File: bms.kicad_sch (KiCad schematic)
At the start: 62 parts, among them J10 SOLAR, Q10 SI2308, Q11 CSD17577Q3A, Q7 CSD18512Q5B, Q8 CSD18512Q5B, Q9 SI2308, SW3 POWER/RESET, U8 BQ25798

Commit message: lots of fixes!
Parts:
- removed C134: 10nF, Capacitor_SMD:C_0402_1005Metric, symbol Device:C_Small
- removed C35, C57, C59, C60, C63, C65, C71, C73, C74, C82, C84, C85, C86, C87, C88, C90, C92: 10uF, Capacitor_SMD:C_1206_3216Metric, symbol Device:C_Small
- removed C62, C79: 2.2uF, Capacitor_SMD:C_0805_2012Metric, symbol Device:C_Small
- removed C64, C72, C80, C89, C91: 100nF, Capacitor_SMD:C_0402_1005Metric, symbol Device:C_Small
- removed C75, C76, C77: 47nF, Capacitor_SMD:C_0402_1005Metric, symbol Device:C_Small
- removed C78: 4.7uF, Capacitor_SMD:C_0603_1608Metric, symbol Device:C_Small
- removed C81, C83: 1nF, Capacitor_SMD:C_0402_1005Metric_Pad0.74x0.62mm_HandSolder, symbol Device:C_Small
- removed D7: SMF24A, Diode_SMD:D_SOD-123F, symbol Diode:SMF24A
- removed D8: CHARGING, LED_SMD:LED_0805_2012Metric, symbol Device:LED
- removed D9: SS36B, Diode_SMD:D_SMB, symbol Device:D_Schottky
- removed J10: SOLAR, Connector_JST:JST_PH_S2B-PH-SM4-TB_1x02-1MP_P2.00mm_Horizontal, symbol Connector:Conn_01x02_Socket
- removed L1: 2.2uH, Inductor_SMD:L_Vishay_IFSC-1515AH_4x4x1.8mm, symbol Device:L
- removed Q10, Q9: SI2308, Package_TO_SOT_SMD:SOT-23, symbol Transistor_FET:Q_NMOS_GSD
- removed Q11: CSD17577Q3A, Package_SON:VSON-8_3.3x3.3mm_P0.65mm_NexFET, symbol Transistor_FET:CSD17581Q3A
- removed Q7, Q8: CSD18512Q5B, Package_SON:VSONP-8-1EP_5x6_P1.27mm, symbol Transistor_FET:Q_NMOS_DGS
- removed R49, R62: 2, Resistor_SMD:R_0402_1005Metric, symbol Device:R_Small
- removed R51: 5.23k, Resistor_SMD:R_0603_1608Metric_Pad0.98x0.95mm_HandSolder, symbol Device:R_Small
- removed R52: 30.1k, Resistor_SMD:R_0603_1608Metric_Pad0.98x0.95mm_HandSolder, symbol Device:R_Small
- removed R53, R57, R60, R61: 294, Resistor_SMD:R_0402_1005Metric, symbol Device:R_Small
- removed R54: 24.3k, Resistor_SMD:R_0603_1608Metric_Pad0.98x0.95mm_HandSolder, symbol Device:R_Small
- removed R55: 68.1k, Resistor_SMD:R_0603_1608Metric_Pad0.98x0.95mm_HandSolder, symbol Device:R_Small
- removed R56: 100k, Resistor_SMD:R_0402_1005Metric, symbol Device:R_Small
- removed R58: 8.2k, Resistor_SMD:R_0402_1005Metric_Pad0.72x0.64mm_HandSolder, symbol Device:R_Small
- removed R59, R63: 100, Resistor_SMD:R_0402_1005Metric, symbol Device:R_Small
- removed R64, R65: 2.2, Resistor_SMD:R_0402_1005Metric_Pad0.72x0.64mm_HandSolder, symbol Device:R_Small
- removed R66: 3k, Resistor_SMD:R_0402_1005Metric_Pad0.72x0.64mm_HandSolder, symbol Device:R_Small
- removed SW3: POWER/RESET, Button_Switch_SMD:SW_Push_SPST_NO_Alps_SKRK, symbol Switch:SW_Push
- removed TH5: 103AT 10k, Resistor_SMD:R_0603_1608Metric, symbol Device:Thermistor_NTC
- removed TP4: PPHV, TestPoint:TestPoint_2Pads_Pitch2.54mm_Drill0.8mm, symbol Connector:TestPoint_2Pole
- removed U8: BQ25798, Package_DFN_QFN:Texas_RQM0029A_VQFN-29_4x4mm_P0.4mm, symbol Battery_Management:BQ25798
- added BT1, BT2: 21700 Li-ion, easyeda2kicad:BAT-SMD_L82.5.5-W25-BH-21700-B1BJ001, symbol Device:Battery_Cell
- added C105, C132, C47, C98: 10nF, Capacitor_SMD:C_0402_1005Metric, symbol Device:C_Small
- added C48, C67, C68, C69, C70: 10uF, Capacitor_SMD:C_0805_2012Metric, symbol Device:C_Small
- added C49, C50, C51, C54, C61, C66: 100nF, Capacitor_SMD:C_0402_1005Metric, symbol Device:C_Small
- added C52: 1uF, Capacitor_SMD:C_0402_1005Metric, symbol Device:C_Small
- added C53, C55, C56, C58: 0.47uF, Capacitor_SMD:C_0402_1005Metric, symbol Device:C_Small
- added D23: BAT54S, Package_TO_SOT_SMD:SOT-23, symbol Diode:BAT54S
- added D5: SMF10A, Diode_SMD:D_SOD-123, symbol Diode:SMF10A
- added D6: BZX585-C15,135, Diode_SMD:D_SOD-523, symbol Device:D_Zener
- added F5: 10A hold, Fuse:Fuse_2920_7451Metric, symbol Device:Polyfuse
- added J9: BAT_PORT, Connector_Molex:Molex_PicoBlade_53261-0271_1x02-1MP_P1.25mm_Horizontal, symbol Connector_Generic_MountingPin:Conn_01x02_MountingPin
- added JP7: ZVC, Jumper:SolderJumper-2_P1.3mm_Open_RoundedPad1.0x1.5mm, symbol Jumper:SolderJumper_2_Open
- added Q16: TPN2R203NC, easyeda2kicad:TSON-8_L3.1-W3.1-P0.65-LS3.3-BL-EP, symbol Transistor_FET:CSD17581Q3A
- added Q5, Q6: AON7544, easyeda2kicad:PQFN-8_L3.1-W3.1-P0.65-LS3.3-BL, symbol easyeda2kicad:AON7534-ES
- added R135, R46, R50: 10k, Resistor_SMD:R_0402_1005Metric, symbol Device:R_Small
- added R39, R40: 150, Resistor_SMD:R_1206_3216Metric, symbol Device:R_Small
- added R41: 5m, footprints:R_Shunt_0805_2012Metric_Kelvin, symbol Device:R_Shunt
- added R42: 10, Resistor_SMD:R_0402_1005Metric, symbol Device:R_Small
- added R43, R45: 1k, Resistor_SMD:R_0402_1005Metric, symbol Device:R_Small
- added R44, R48: 100, Resistor_SMD:R_0402_1005Metric, symbol Device:R_Small
- added R47: 330, Resistor_SMD:R_1210_3225Metric, symbol Device:R_Small
- added TH1, TH2, TH3, TH4: 103AT 10k, Resistor_SMD:R_0603_1608Metric, symbol Device:Thermistor_NTC
- added TP1: R_SENSE_SHUNT, TestPoint:TestPoint_2Pads_Pitch2.54mm_Drill0.8mm, symbol Connector:TestPoint_2Pole
- added TP2: IN_CP, TestPoint:TestPoint_2Pads_Pitch2.54mm_Drill0.8mm, symbol Connector:TestPoint_2Pole
- added TP3: REG3, TestPoint:TestPoint_Pad_D1.0mm, symbol Connector:TestPoint_Probe
- added U7: MAX17320G22+, easyeda2kicad:QFN-24_L4.0-W4.0-P0.50-BL-EP2.6, symbol easyeda2kicad:MAX17320G22+
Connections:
- net +PACK: now also C61.2, C66.1, C67.1, C68.1, C69.1, C70.1, Q6.1 (S), Q6.2 (S), Q6.3 (S), R45.2, R47.2
- net GND: now also C67.2, C68.2, C69.2, C70.2, R41.4, TP1.2
- new net: C98.1, TH1.1, U7.16 (TH2)
- new net: BT2.2 (-), J9.1 (Pin_1), Q16.5 (D), Q16.6 (D), Q16.7 (D), Q16.8 (D), Q16.9 (D)
- new net: BT1.1 (+), F5.1, J9.2 (Pin_2), R135.1, R40.1, R42.1
- new net: JP7.1 (A), U7.5 (ZVC)
- new net: JP7.2 (B), R47.1
- new net: R48.1, U7.4 (DIS)
- new net: Q6.4 (G), R48.2
- new net: C56.2, TP3.1, U7.13 (REG3)
- new net: C47.1, TH4.1, U7.10 (TH1)
- new net: D6.1 (K), Q16.4 (G), R135.2
- new net: C105.1, TH3.1, U7.18 (TH3)
- new net: R50.1, U7.7 (ALRT)
- new net: C132.1, TH2.1, U7.19 (TH4)
- new net: BT1.2 (-), BT2.1 (+), R39.1
- new net: C49.2, C50.1, D23.3 (COM), R39.2, U7.21 (CELL1)
- new net: R45.1, U7.6 (PCKP)
- new net: R43.1, U7.11 (PFAIL)
- new net: C58.1, R46.1, U7.12 (AOLDO)
- new net: R41.3, U7.14 (CSN)
- new net: R41.2, U7.15 (CSP)
- new net: C55.2, U7.17 (REG2)
- new net: C53.2, TP2.2, U7.2 (CP)
- new net: C49.1, C51.1, R40.2, U7.22 (CELL2), U7.23 (CELL3), U7.24 (BATTS)
- new net: R44.1, U7.3 (CHG)
- new net: Q5.5 (D), Q5.6 (D), Q5.7 (D), Q5.8 (D), Q6.5 (D), Q6.6 (D), Q6.7 (D), Q6.8 (D)
- new net: C54.2, Q5.4 (G), R44.2
- new net +3V3: R50.2
- new net +BATT: C48.1, C54.1, C61.1, D5.1 (A1), F5.2, Q5.1 (S), Q5.2 (S), Q5.3 (S)
- new net -BATT: C105.2, C132.2, C47.2, C48.2, C50.2, C51.2, C52.2, C55.1, C56.1, C58.2, C66.2, C98.2, D23.1 (A), D5.2 (A2), D6.2 (A), Q16.1 (S), Q16.2 (S), Q16.3 (S), R41.1, R43.2, R46.2, TH1.2, TH2.2, TH3.2, TH4.2, TP1.1, U7.20 (GND), U7.25 (EP)
- new net BMS_IN: C52.1, C53.1, D23.2 (K), R42.2, TP2.1, U7.1 (IN)
- new net I2C_HOST_SCL: U7.8 (SCL/DOD)
- new net I2C_HOST_SDA: U7.9 (SDA/DQ)
- no-connect marks 2 -> 1
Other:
- note added: "10nF noise filtering capacitors"
- note added: "Battery Management System (BMS)"
- note removed: "4 x 10uF 1206"
- note removed: "5 x 10uF 1210"
- note removed: "Capacitors voltage ratings specified, generally >25V - use XR7/C0G"
- note removed: "Charge Controller"
- note removed: "VSYS from 7.1V - 8.8V for 2S, max ~6A"
- title: Battery Charge Controller -> Battery Managment System (BMS)

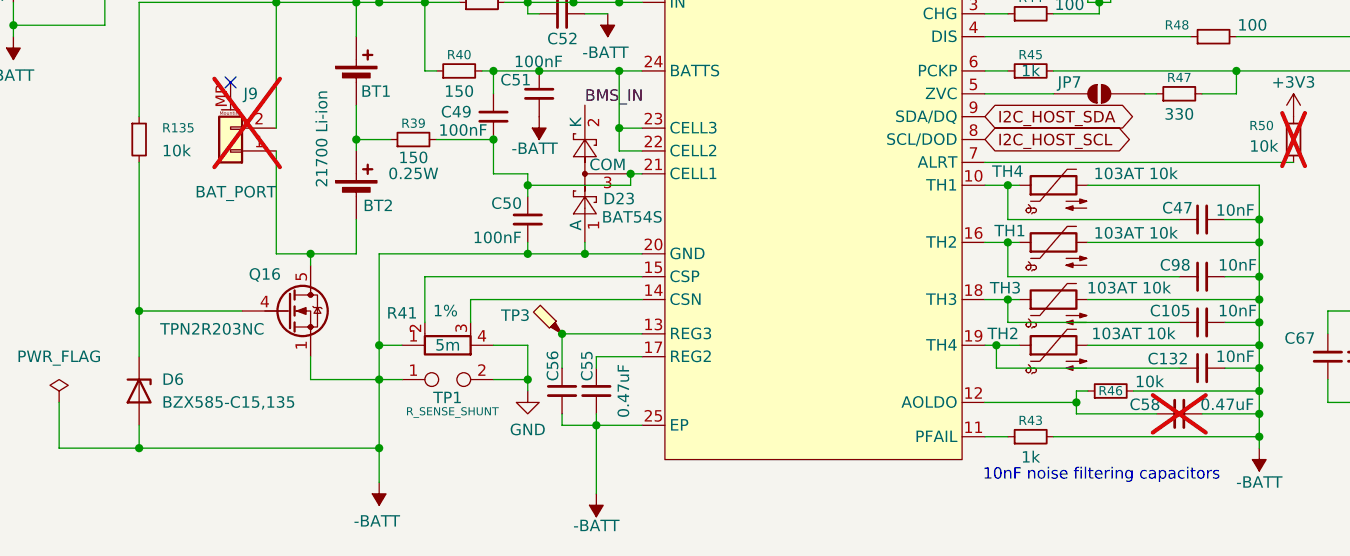
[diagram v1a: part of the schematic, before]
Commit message: organize part fields
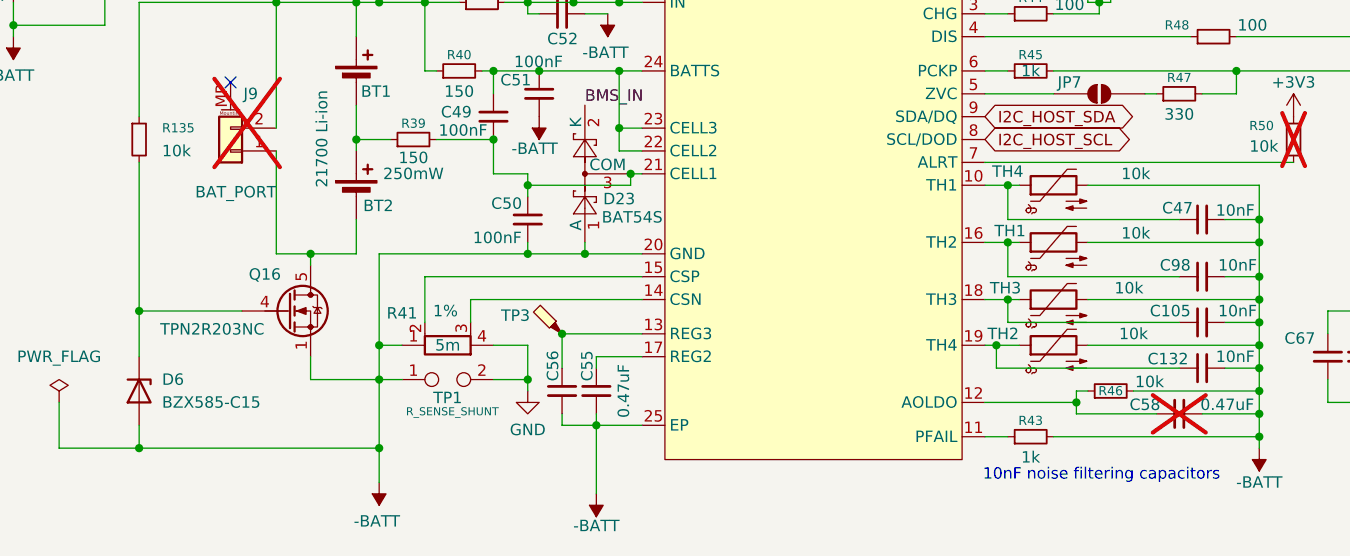
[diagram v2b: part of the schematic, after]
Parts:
- BT1, BT2: MPN (none) -> BH-21700-B1BJ001; Manufacturer (none) -> MYOUNG
- C105, C132, C47, C98: Dielectric (none) -> X7R; MPN (none) -> TCC0402X7R103M500AT; Manufacturer (none) -> CCTC; Tolerance (none) -> 20%
- C48: Dielectric (none) -> X5R; MPN (none) -> CGA0805X5R106M500MT; Manufacturer (none) -> HRE; Tolerance (none) -> 20%
- C49, C51, C61, C66: Capacitor Rating X7R -> (none); Dielectric (none) -> X7R; MPN (none) -> 0402B104J500NT; Manufacturer (none) -> FH (Fenghua); Tolerance (none) -> 5%
- C50, C54: Capacitor Rating X7R -> (none); Dielectric (none) -> X7R; MPN (none) -> 0402B104J500NT; Manufacturer (none) -> FH (Fenghua); Tolerance (none) -> 5%; Voltage Rating 25V -> 50V
- C52: Dielectric (none) -> X5R; MPN (none) -> HGC0402R5105K500NTEJ; Manufacturer (none) -> Chinocera; Tolerance (none) -> 10%
- C53, C55: Dielectric (none) -> X5R; MPN (none) -> HGC0402R5474K250NTEJ; Manufacturer (none) -> Chinocera; Tolerance (none) -> 10%
- C56, C58: Dielectric (none) -> X5R; MPN (none) -> HGC0402R5474K250NTEJ; Manufacturer (none) -> Chinocera; Tolerance (none) -> 10%; Voltage Rating 16V -> 25V
- C67, C68, C69, C70: Dielectric (none) -> X5R; MPN (none) -> CGA0805X5R106M500MT; Manufacturer (none) -> HRE; Tolerance (none) -> 20%; Voltage Rating 25V -> 50V
- D23: MPN (none) -> BAT54SLT1G; Manufacturer (none) -> onsemi
- D5: MPN (none) -> SMF10A; Manufacturer (none) -> AnBon
- D6: value BZX585-C15,135 -> BZX585-C15; MPN (none) -> BZX585-C15,135; Manufacturer (none) -> Nexperia
- F5: MPN (none) -> BSMD2920L-1000-21V; Manufacturer (none) -> BHFUSE
- J9: MPN (none) -> 1.25-2PWB; Manufacturer (none) -> DEALON
- Q16: MPN (none) -> TPN2R203NC,L1Q(M; Manufacturer (none) -> Toshiba
- Q5, Q6: Manufacturer (none) -> Alpha & Omega Semiconductor
- R135, R46, R50: MPN (none) -> FRH0402D1002TS; Manufacturer (none) -> FOJAN; Power Rating (none) -> 62.5mW; Tolerance (none) -> 0.5%
- R39: MPN (none) -> RT1206BRD07150RL; Manufacturer (none) -> YAGEO; Power Rating 0.25W -> 250mW; Tolerance (none) -> 0.1%
- R40: MPN (none) -> RT1206BRD07150RL; Manufacturer (none) -> YAGEO; Power Rating (none) -> 250mW; Tolerance (none) -> 0.1%
- R41: MPN (none) -> YHR0805SE1DR005F5; Manufacturer (none) -> Yohey; Power Rating (none) -> 500mW
- R42: MPN (none) -> 1RC0402F1009; Manufacturer (none) -> SAE; Power Rating (none) -> 62.5mW; Tolerance (none) -> 1%
- R43, R45: MPN (none) -> FRH0402B1001TS; Manufacturer (none) -> FOJAN; Power Rating (none) -> 62.5mW; Tolerance (none) -> 0.1%
- R44, R48: MPN (none) -> FRH0402D1000TS; Manufacturer (none) -> FOJAN; Power Rating (none) -> 62.5mW; Tolerance (none) -> 0.5%
- R47: MPN (none) -> FRP1210F3300TS; Manufacturer (none) -> FOJAN; Tolerance (none) -> 1%
- TH1, TH2, TH3, TH4: value 103AT 10k -> 10k; MPN (none) -> NCU18XH103D60RB; Manufacturer (none) -> Murata; Tolerance (none) -> 0.5%
- U7: Manufacturer ADI(亚德诺)/MAXIM(美信) -> Analog Devices (Maxim)

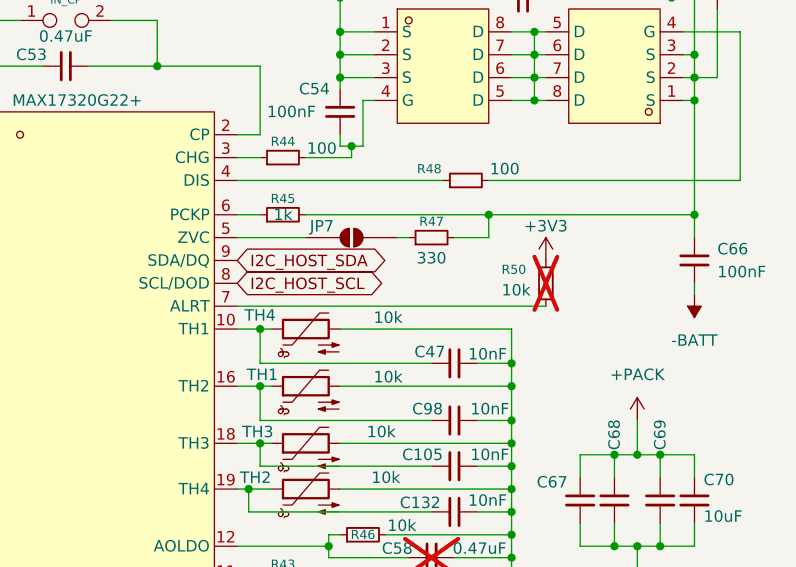
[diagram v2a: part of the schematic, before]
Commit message: add extra PWR_FLAGs
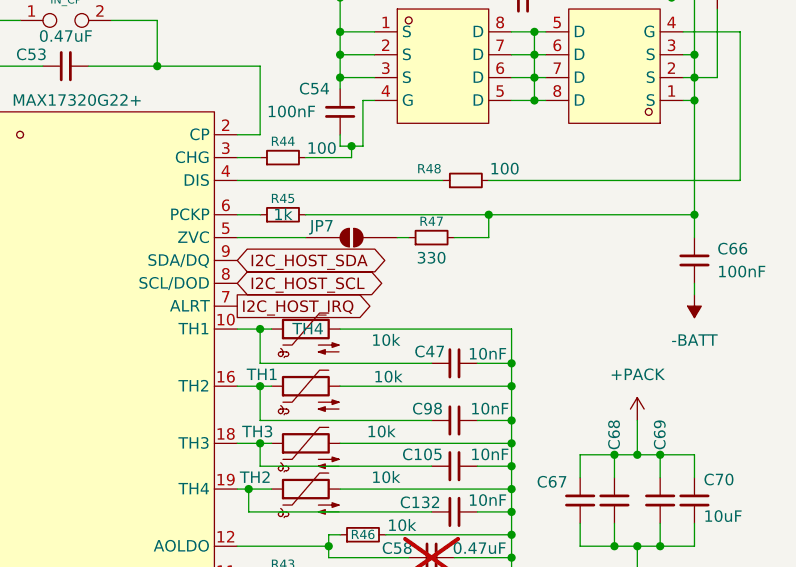
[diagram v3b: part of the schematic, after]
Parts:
- removed R50: 10k, Resistor_SMD:R_0402_1005Metric, symbol Device:R_Small
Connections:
- net I2C_HOST_IRQ: now reaches U7.7 (ALRT)
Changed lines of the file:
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@@
 	(wire
 		(pts
-			(xy 205.74 104.14) (xy 171.45 104.14)
-		)
-		(stroke
-			(width 0)
-			(type default)
-		)
-	)
-	(wire
-		(pts
 			(xy 116.84 93.98) (xy 116.84 96.52)
 		)
@@
 		)
 	)
+	(global_label "I2C_HOST_IRQ"
+		(shape output)
+		(at 171.45 104.14 0)
+		(fields_autoplaced yes)
+		(effects
+			(font
+				(size 1.27 1.27)
+			)
+			(justify left)
+		)
+		(property "Intersheetrefs" "${INTERSHEET_REFS}"
+			(at 187.4981 104.14 0)
+			(hide yes)
+			(show_name no)
+			(do_not_autoplace no)
+			(effects
+				(font
+					(size 1.27 1.27)
+				)
+				(justify left)
+			)
+		)
+	)
 	(global_label "I2C_HOST_SDA"
 		(shape bidirectional)
@@
 	)
 	(symbol
-		(lib_id "Device:R_Small")
-		(at 205.74 101.6 180)
-		(unit 1)
-		(body_style 1)
-		(exclude_from_sim no)
-		(in_bom yes)
-		(on_board yes)
-		(in_pos_files yes)
-		(dnp yes)
-		(property "Reference" "R50"
-			(at 202.184 100.076 0)
-			(show_name no)
-			(do_not_autoplace no)
-			(effects
-				(font
-					(size 1.016 1.016)
-				)
-			)
-		)
-		(property "Value" "10k"
-			(at 202.438 102.362 0)
-			(show_name no)
-			(do_not_autoplace no)
-			(effects
-				(font
-					(size 1.27 1.27)
-				)
-			)
-		)
-		(property "Footprint" "Resistor_SMD:R_0402_1005Metric"
-			(at 205.74 101.6 0)
-			(hide yes)
-			(show_name no)
-			(do_not_autoplace no)
-			(effects
-				(font
-					(size 1.27 1.27)
-				)
-			)
-		)
-		(property "Datasheet" "https://datasheet.lcsc.com/datasheet/pdf/68379ec060dbf46ca58f0ea52f41dfcd.pdf?productCode=C54951138"
-			(at 205.74 101.6 0)
-			(hide yes)
-			(show_name no)
-			(do_not_autoplace no)
-			(effects
-				(font
-					(size 1.27 1.27)
-				)
-			)
-		)
-		(property "Description" "RES 10kΩ ±0.5% 62.5mW 0402 thick film"
-			(at 205.74 101.6 0)
-			(hide yes)
-			(show_name no)
-			(do_not_autoplace no)
-			(effects
-				(font
-					(size 1.27 1.27)
-				)
-			)
-		)
-		(property "MPN" "FRH0402D1002TS"
-			(at 205.74 101.6 0)
-			(hide yes)
-			(show_name no)
-			(do_not_autoplace no)
-			(effects
-				(font
-					(size 1.27 1.27)
-				)
-			)
-		)
-		(property "Manufacturer" "FOJAN"
-			(at 205.74 101.6 0)
-			(hide yes)
-			(show_name no)
-			(do_not_autoplace no)
-			(effects
-				(font
-					(size 1.27 1.27)
-				)
-			)
-		)
-		(property "LCSC Part" "C54951138"
-			(at 205.74 101.6 0)
-			(hide yes)
-			(show_name no)
-			(do_not_autoplace no)
-			(effects
-				(font
-					(size 1.27 1.27)
-				)
-			)
-		)
-		(property "Tolerance" "0.5%"
-			(at 205.74 101.6 0)
-			(hide yes)
-			(show_name no)
-			(do_not_autoplace no)
-			(effects
-				(font
-					(size 1.27 1.27)
-				)
-			)
-		)
-		(property "Power Rating" "62.5mW"
-			(at 205.74 101.6 0)
-			(hide yes)
-			(show_name no)
-			(do_not_autoplace no)
-			(effects
-				(font
-					(size 1.27 1.27)
-				)
-			)
-		)
-		(pin "1"
-		)
-		(pin "2"
-		)
-		(instances
-			(project "parsnip"
-				(path "/9f6a091f-857b-49d0-a04b-55dd2f7de6dd"
-					(reference "R50")
-					(unit 1)
-				)
-			)
-		)
-	)
-	(symbol
 		(lib_id "Device:Thermistor_NTC")
 		(at 179.07 124.46 90)
@@
 		(dnp no)
 		(property "Reference" "TH4"
-			(at 173.99 105.156 90)
+			(at 179.324 106.68 90)
 			(show_name no)
 			(do_not_autoplace no)
@@
 		)
 		(property "Value" "10k"
-			(at 188.214 105.41 90)
+			(at 187.96 107.95 90)
 			(show_name no)
 			(do_not_autoplace no)
@@
 					(unit 1)
 				)
-			)
-		)
-	)
-	(symbol
-		(lib_id "power:+3V3")
-		(at 205.74 99.06 0)
-		(unit 1)
-		(body_style 1)
-		(exclude_from_sim no)
-		(in_bom yes)
-		(on_board yes)
-		(in_pos_files yes)
-		(dnp no)
-		(property "Reference" "#PWR069"
-			(at 205.74 102.87 0)
-			(hide yes)
-			(show_name no)
-			(do_not_autoplace no)
-			(effects
-				(font
-					(size 1.27 1.27)
-				)
-			)
-		)
-		(property "Value" "+3V3"
-			(at 205.74 95.25 0)
-			(show_name no)
-			(do_not_autoplace no)
-			(effects
-				(font
-					(size 1.27 1.27)
-				)
-			)
-		)
-		(property "Footprint" ""
-			(at 205.74 99.06 0)
-			(hide yes)
-			(show_name no)
-			(do_not_autoplace no)
-			(effects
-				(font
-					(size 1.27 1.27)
-				)
-			)
-		)
-		(property "Datasheet" ""
-			(at 205.74 99.06 0)
-			(hide yes)
-			(show_name no)
-			(do_not_autoplace no)
-			(effects
-				(font
-					(size 1.27 1.27)
-				)
-			)
-		)
-		(property "Description" "Power symbol creates a global label with name \"+3V3\""
-			(at 205.74 99.06 0)
-			(hide yes)
-			(show_name no)
-			(do_not_autoplace no)
-			(effects
-				(font
-					(size 1.27 1.27)
-				)
-			)
-		)
-		(pin "1"
-		)
-		(instances
-			(project "parsnip"
-				(path "/9f6a091f-857b-49d0-a04b-55dd2f7de6dd"
-					(reference "#PWR069")
-					(unit 1)
-				)

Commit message: nearly set to order!
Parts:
- removed R39, R40: 150, Resistor_SMD:R_1206_3216Metric, symbol Device:R_Small
- added R39, R40: 150, Resistor_SMD:R_1206_3216Metric, symbol Device:R
- F5: value 10A hold -> 10A Hold
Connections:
- net -BATT: now also C58.1, R46.1; no longer C58.2, R46.2
- net at C98.1, TH1.1: now also U7.10 (TH1); no longer U7.16 (TH2)
- net at C47.1, TH4.1: now also U7.19 (TH4); no longer U7.10 (TH1)
- net at D6.1 (K), Q16.4 (G): now also R135.1; no longer R135.2
- net at C132.1, TH2.1: now also U7.16 (TH2); no longer U7.19 (TH4)
- net at BT1.2 (-), BT2.1 (+): now also R39.1
- net at C49.2, C50.1, D23.3 (COM)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: now also R39.2
- net at C49.1, C51.1, U7.22 (CELL2)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: now also R40.2
- new net: BT1.1 (+), J9.2 (Pin_2), R135.2, R40.1
- new net: C58.2, R46.2, U7.12 (AOLDO)
- new net: F5.1, R42.1
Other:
- note added: "20A Trip"
- note added: "4 x 10uF 50V"
- note removed: "10nF noise filtering capacitors"
- moved on the sheet: C53, C61, C66, C67, C68, C69, C70, C98, Q5, Q6, R47, TH1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
